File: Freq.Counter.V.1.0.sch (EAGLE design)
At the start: 15 parts, among them IC1 MEGA8-P, IC2 7805TV, IC3 74HC93N, Q1 16M

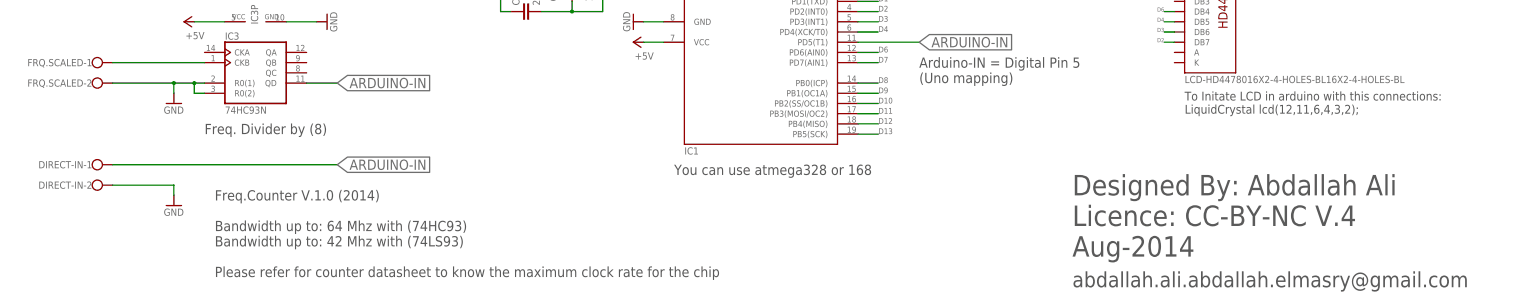
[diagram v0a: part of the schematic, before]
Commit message: Arduino Freq. Counter (up to 64 Mhz) V.1.1
Arduino Freq. Counter (up to 64 Mhz) V.1.1
With smaller PCB
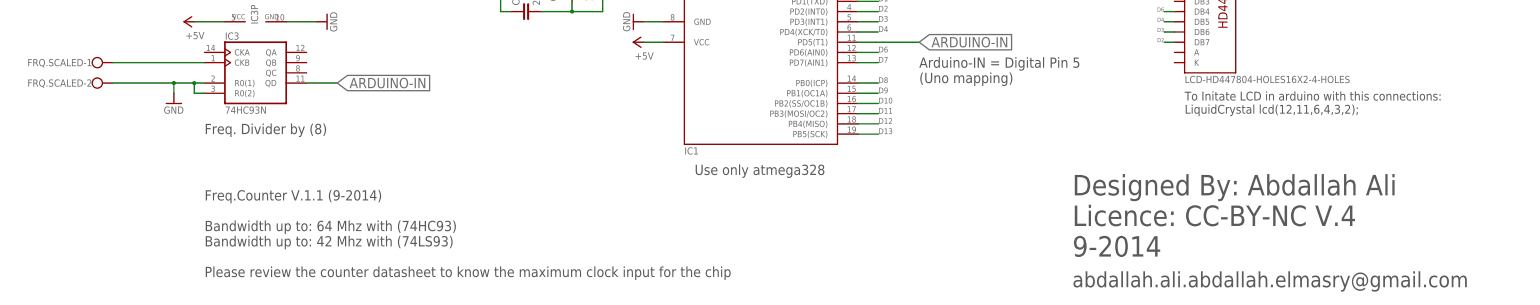
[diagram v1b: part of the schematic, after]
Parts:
- removed DIRECT-IN: (no value), con-wago-500:W237-102
- C1, C2: device rcl:C-EU050-025X075 -> rcl:C-EU025-025X050
- U$1: value LCD-HD4478016X2-4-HOLES-BL16X2-4-HOLES-BL -> LCD-HD447804-HOLES16X2-4-HOLES; device HD44780LCD:LCD-HD4478016X2-4-HOLES-BL16X2-4-HOLES-BL -> LCD-Library-EagleCAD-HD44780:LCD-HD447804-HOLES16X2-4-HOLES
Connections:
- net ARDUINO-IN: no longer DIRECT-IN-1.KL
- net GND: no longer DIRECT-IN-2.KL
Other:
- note added: "Designed By: Abdallah Ali Licence: CC-BY-NC V.4 9-2014"
- note added: "Freq.Counter V.1.1 (9-2014) Bandwidth up to: 64 Mhz with (74HC93) Bandwidth up to: 42 Mhz with (74LS93) Please review the counter datasheet to know the maximum clock input for the chip"
- note added: "Use only atmega328"
- note removed: "Designed By: Abdallah Ali Licence: CC-BY-NC V.4 Aug-2014"
- note removed: "Freq.Counter V.1.0 (2014) Bandwidth up to: 64 Mhz with (74HC93) Bandwidth up to: 42 Mhz with (74LS93) Please refer for counter datasheet to know the maximum clock rate for the chip"
- note removed: "You can use atmega328 or 168"
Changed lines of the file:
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@@
 <?xml version="1.0" encoding="utf-8"?>
 <!DOCTYPE eagle SYSTEM "eagle.dtd">
-<eagle version="6.5.0">
+<eagle version="6.3">
 <drawing>
 <settings>
@@
 <part name="IC1" library="atmel" deviceset="MEGA8-P" device=""/>
 <part name="R1" library="rcl" deviceset="R-US_" device="0207/10" value="10k"/>
-<part name="IC2" library="linear" deviceset="78*" device="TV" technology="05"/>
+<part name="IC2" library="linear" deviceset="78*" device="TV" technology="05" value="7805TV"/>
 <part name="RESET" library="switch-omron" deviceset="10-XX" device=""/>
 <part name="+5V" library="pinhead" deviceset="PINHD-1X2" device=""/>
@@
 <part name="IC3" library="74xx-eu" deviceset="74*93" device="N" technology="HC"/>
 <part name="GND7" library="supply1" deviceset="GND" device=""/>
-<part name="GND8" library="supply1" deviceset="GND" device=""/>
-<part name="U$1" library="HD44780LCD" deviceset="LCD-HD44780" device="16X2-4-HOLES-BL" technology="16X2-4-HOLES-BL"/>
+<part name="U$1" library="LCD-Library-EagleCAD-HD44780" deviceset="LCD-HD44780" device="16X2-4-HOLES" technology="4-HOLES" value="LCD-HD447804-HOLES16X2-4-HOLES"/>
 <part name="GND9" library="supply1" deviceset="GND" device=""/>
 <part name="P+8" library="supply1" deviceset="+5V" device=""/>
@@
 <part name="POWER-IT" library="con-wago-500" deviceset="W237-102" device=""/>
 <part name="FRQ.SCALED" library="con-wago-500" deviceset="W237-102" device=""/>
-<part name="DIRECT-IN" library="con-wago-500" deviceset="W237-102" device=""/>
 <part name="Q1" library="special" deviceset="XTAL/S" device="" value="16M"/>
-<part name="C1" library="rcl" deviceset="C-EU" device="050-025X075" value="22p"/>
-<part name="C2" library="rcl" deviceset="C-EU" device="050-025X075" value="22p"/>
+<part name="C1" library="rcl" deviceset="C-EU" device="025-025X050" value="22p"/>
+<part name="C2" library="rcl" deviceset="C-EU" device="025-025X050" value="22p"/>
 <part name="GND11" library="supply1" deviceset="GND" device=""/>
 <part name="GND12" library="supply1" deviceset="GND" device=""/>
@@
 <text x="170.18" y="45.72" size="2.1844" layer="92">To Initate LCD in arduino with this connections:
 LiquidCrystal lcd(12,11,6,4,3,2);</text>
-<text x="-71.12" y="5.08" size="2.54" layer="92">Freq.Counter V.1.0 (2014)
+<text x="-73.66" y="5.08" size="2.54" layer="92">Freq.Counter V.1.1 (9-2014)
 Bandwidth up to: 64 Mhz with (74HC93)
 Bandwidth up to: 42 Mhz with (74LS93)
-Please refer for counter datasheet to know the maximum clock rate for the chip</text>
-<text x="43.18" y="30.48" size="2.54" layer="92">You can use atmega328 or 168</text>
+Please review the counter datasheet to know the maximum clock input for the chip</text>
+<text x="48.26" y="30.48" size="2.54" layer="92">Use only atmega328</text>
 <text x="-78.74" y="114.3" size="2.54" layer="92">Power Supply with on/off Switch</text>
 <text x="-73.66" y="40.64" size="2.54" layer="92">Freq. Divider by (8)</text>
@@
 <text x="142.24" y="10.16" size="5.08" layer="92">Designed By: Abdallah Ali
 Licence: CC-BY-NC V.4
-Aug-2014</text>
+9-2014</text>
 <text x="142.24" y="2.54" size="3.81" layer="92">abdallah.ali.abdallah.elmasry@gmail.com</text>
 </plain>
@@
 <instance part="IC3" gate="A" x="-60.96" y="55.88"/>
 <instance part="GND7" gate="1" x="-81.28" y="48.26"/>
-<instance part="GND8" gate="1" x="-81.28" y="22.86"/>
 <instance part="U$1" gate="G$1" x="177.8" y="76.2"/>
 <instance part="GND9" gate="1" x="144.78" y="91.44" rot="R270"/>
@@
 <instance part="FRQ.SCALED" gate="-1" x="-101.6" y="58.42"/>
 <instance part="FRQ.SCALED" gate="-2" x="-101.6" y="53.34"/>
-<instance part="DIRECT-IN" gate="-1" x="-101.6" y="33.02"/>
-<instance part="DIRECT-IN" gate="-2" x="-101.6" y="27.94"/>
 <instance part="Q1" gate="G$1" x="17.78" y="78.74" rot="R90"/>
 <instance part="C1" gate="G$1" x="5.08" y="86.36" rot="R90"/>
@@
 </segment>
 <segment>
-<pinref part="DIRECT-IN" gate="-2" pin="KL"/>
-<pinref part="GND8" gate="1" pin="GND"/>
-<wire x1="-96.52" y1="27.94" x2="-81.28" y2="27.94" width="0.1524" layer="91"/>
-<wire x1="-81.28" y1="27.94" x2="-81.28" y2="25.4" width="0.1524" layer="91"/>
-</segment>
-<segment>
 <pinref part="C1" gate="G$1" pin="1"/>
 <wire x1="2.54" y1="86.36" x2="0" y2="86.36" width="0.1524" layer="91"/>
@@
 <label x="104.14" y="63.5" size="2.54" layer="95" xref="yes"/>
 </segment>
-<segment>
-<wire x1="-96.52" y1="33.02" x2="-40.64" y2="33.02" width="0.1524" layer="91"/>
-<label x="-40.64" y="33.02" size="2.54" layer="95" xref="yes"/>
-<pinref part="DIRECT-IN" gate="-1" pin="KL"/>
-</segment>
 </net>
 <net name="D0" class="0">
@@
 </sheet>
 </sheets>
+<errors>
+</errors>
 </schematic>
 </drawing>
